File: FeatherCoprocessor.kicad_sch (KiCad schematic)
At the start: 2 parts

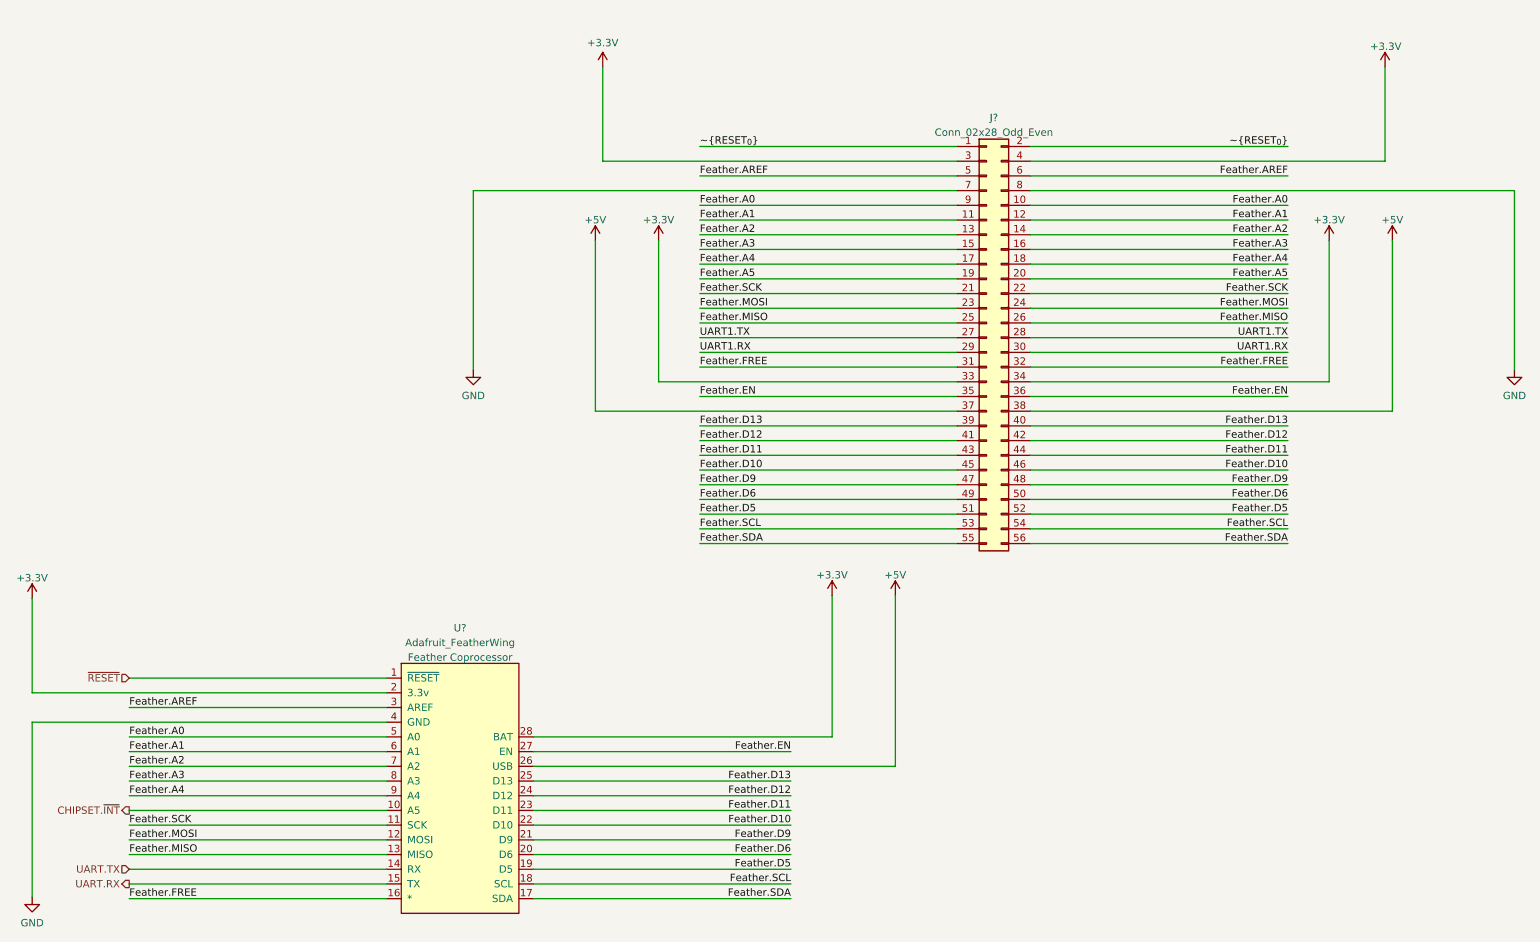
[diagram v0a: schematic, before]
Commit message: Even more simplification and be able to reset feathers separately from the chipset
Makes it possible to also reset them if needed as well
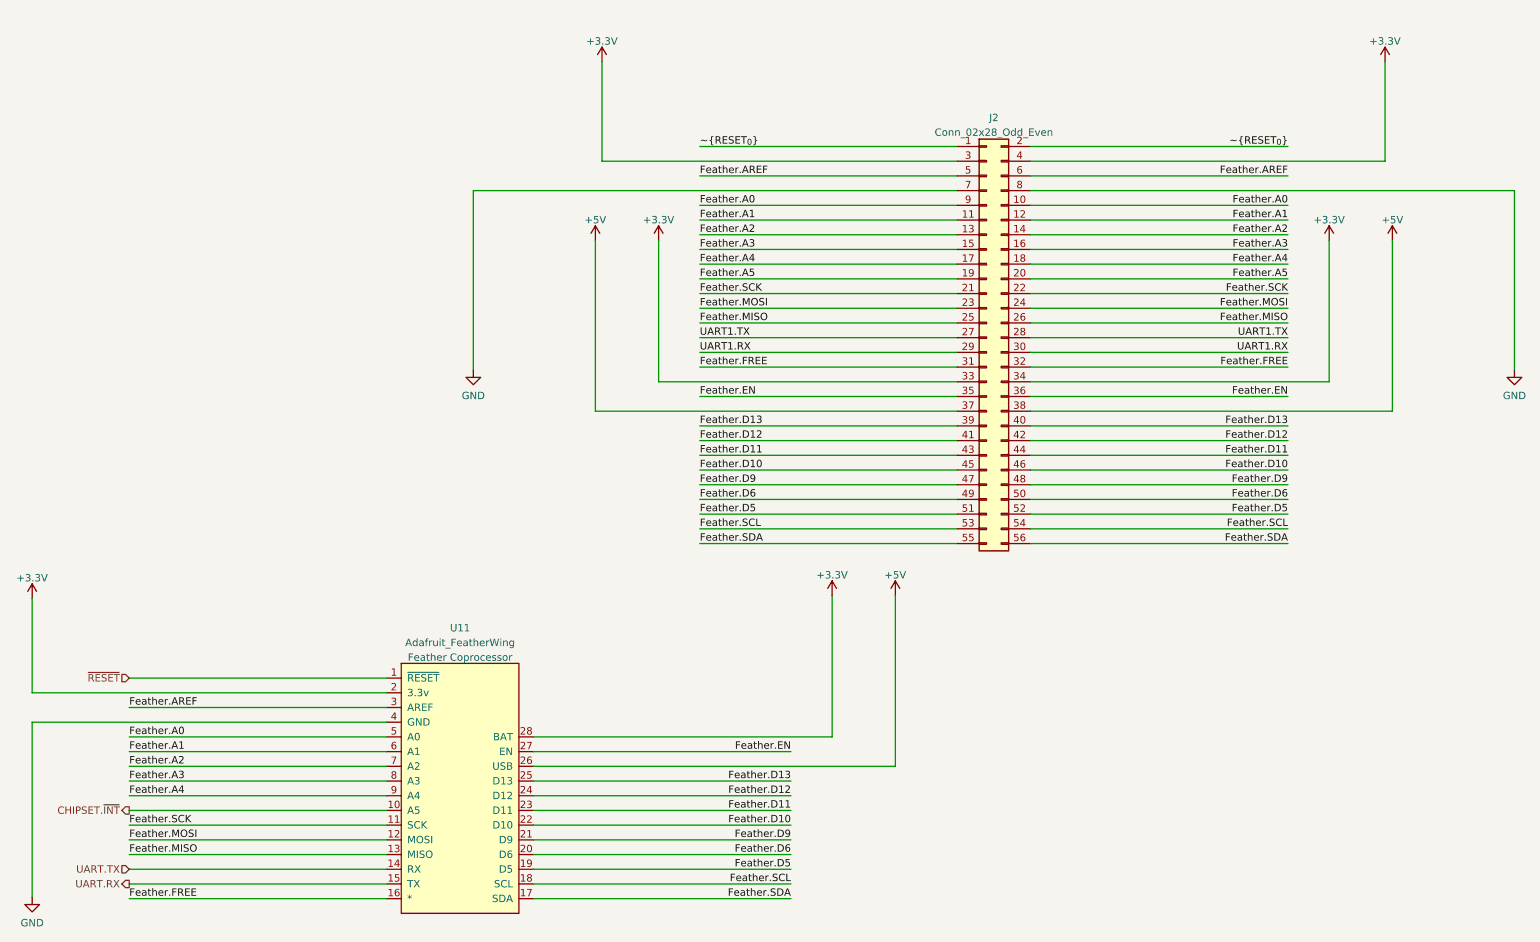
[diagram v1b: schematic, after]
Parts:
- gave numbers to parts that had none: 2
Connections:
- net +3V3 renamed +3.3V

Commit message: Only have one feather
Also came up with a good layout in the form of a "card" style that can
easily be moved around for the i960
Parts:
- removed J2: Conn_02x28_Odd_Even, Connector_PinHeader_2.54mm:PinHeader_2x28_P2.54mm_Vertical, symbol Connector_Generic:Conn_02x28_Odd_Even
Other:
- moved on the sheet: U11

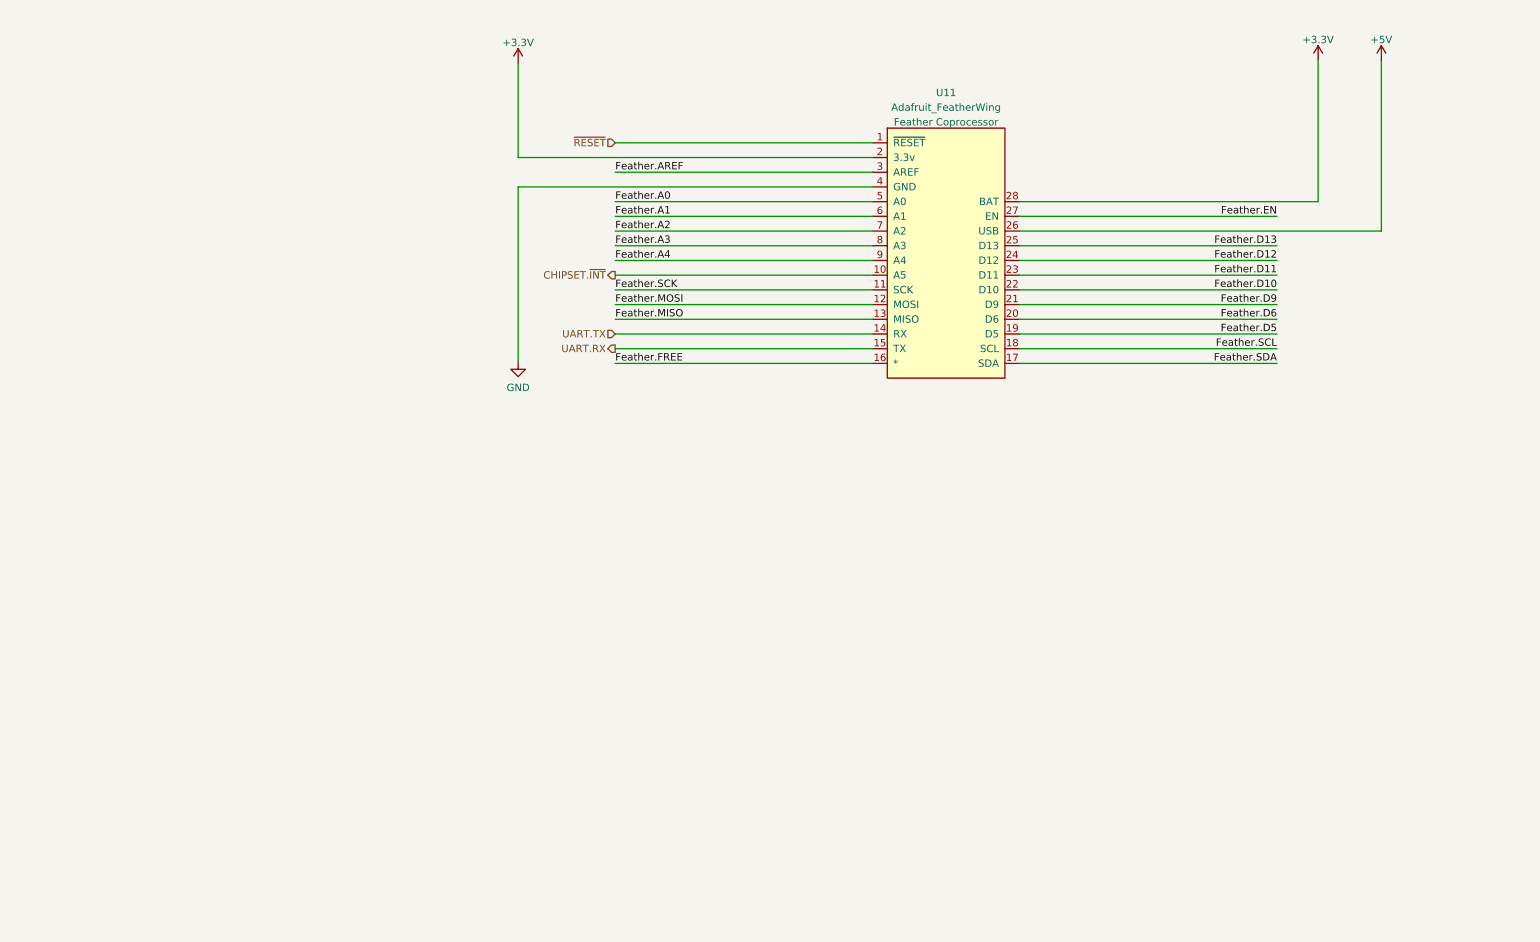
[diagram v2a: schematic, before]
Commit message: Added feather wing sockets next to each plug
F1 has its battery connector blocked by the dazzler shield.

This is not that big of a deal to be honest.
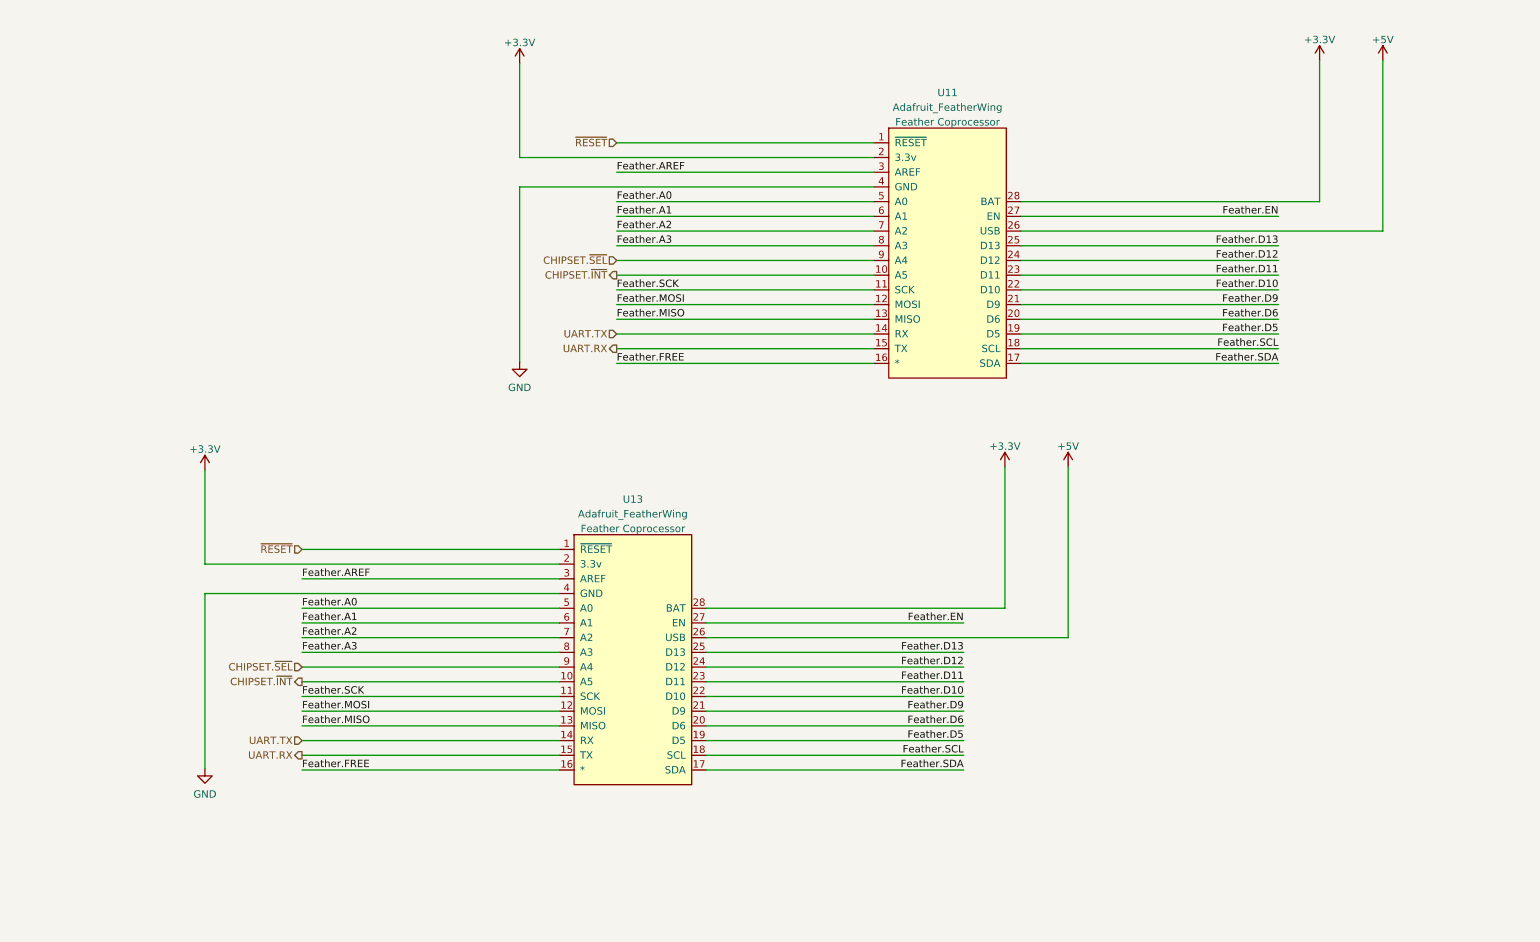
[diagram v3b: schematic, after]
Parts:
- added U13: Adafruit_FeatherWing, Module:Adafruit_Feather, symbol NewICs:Adafruit_FeatherWing
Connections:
- net +3.3V: now also U13.2 (3.3v), U13.28 (BAT)
- net +5V: now also U13.26 (USB)
- net CHIPSET.~{INT}: now also U13.10 (A5)
- net Feather.A0: now also U13.5 (A0)
- net Feather.A1: now also U13.6 (A1)
- net Feather.A2: now also U13.7 (A2)
- net Feather.A3: now also U13.8 (A3)
- net Feather.AREF: now also U13.3 (AREF)
- net Feather.D10: now also U13.22 (D10)
- net Feather.D11: now also U13.23 (D11)
- net Feather.D12: now also U13.24 (D12)
- net Feather.D13: now also U13.25 (D13)
- net Feather.D5: now also U13.19 (D5)
- net Feather.D6: now also U13.20 (D6)
- net Feather.D9: now also U13.21 (D9)
- net Feather.EN: now also U13.27 (EN)
- net Feather.FREE: now also U13.16 (*)
- net Feather.MISO: now also U13.13 (MISO)
- net Feather.MOSI: now also U13.12 (MOSI)
- net Feather.SCK: now also U13.11 (SCK)
- net Feather.SCL: now also U13.18 (SCL)
- net Feather.SDA: now also U13.17 (SDA)
- net GND: now also U13.4 (GND)
- net UART.RX: now also U13.15 (TX)
- net UART.TX: now also U13.14 (RX)
- net ~{RESET}: now also U13.1 (~{RESET})
- net Feather.A4 renamed CHIPSET.~{SEL}
- net CHIPSET.~{SEL}: now also U13.9 (A4)

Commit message: Fix up an issue with 3.3v vs 3v3 power planes
Also, link up more power pads to corresponding power plane
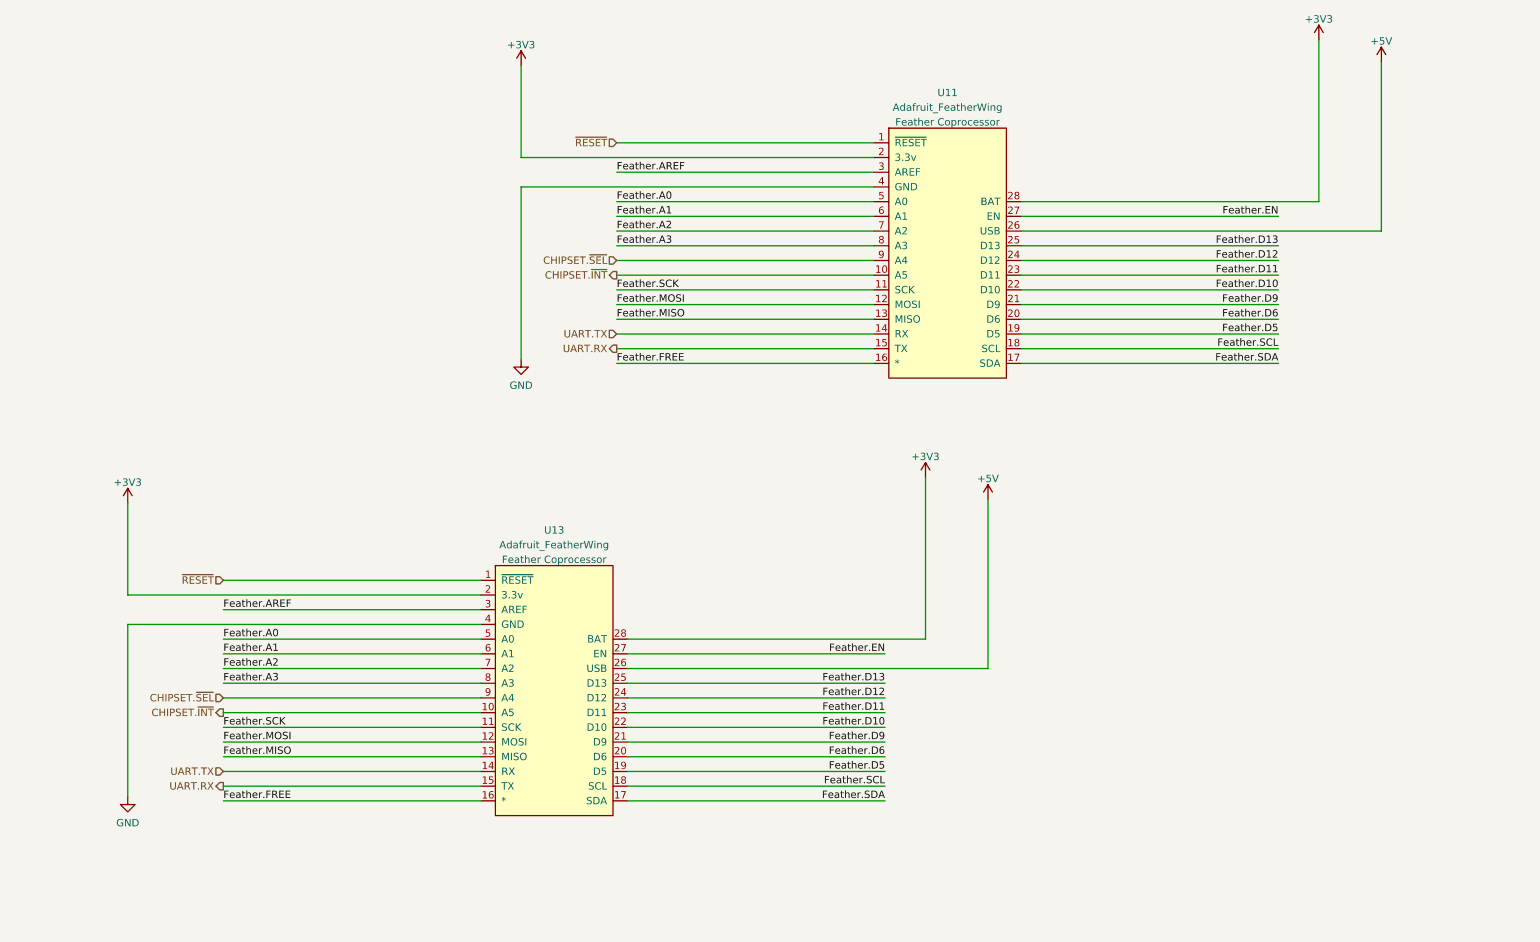
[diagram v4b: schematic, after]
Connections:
- net +3.3V renamed +3V3

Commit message: Added a breakout of the management engine pins
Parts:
- renumbered U13 to U19
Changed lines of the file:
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@@
   (symbol (lib_id "NewICs:Adafruit_FeatherWing") (at 111.76 166.37 0) (unit 1)
     (in_bom yes) (on_board yes) (fields_autoplaced)
-    (property "Reference" "U13" (id 0) (at 111.76 115.8104 0))
+    (property "Reference" "U19" (id 0) (at 111.76 115.8104 0))
     (property "Value" "Adafruit_FeatherWing" (id 1) (at 111.76 118.3473 0))
     (property "Footprint" "Module:Adafruit_Feather" (id 2) (at 111.76 166.37 0)
@@
   (symbol (lib_id "power:GND") (at 38.1 161.925 0) (unit 1)
     (in_bom yes) (on_board yes) (fields_autoplaced)
-    (property "Reference" "#PWR07" (id 0) (at 38.1 168.275 0)
+    (property "Reference" "#PWR015" (id 0) (at 38.1 168.275 0)
       (effects (font (size 1.27 1.27)) hide)
     )
@@
   (symbol (lib_id "power:+5V") (at 186.69 110.49 0) (unit 1)
     (in_bom yes) (on_board yes) (fields_autoplaced)
-    (property "Reference" "#PWR011" (id 0) (at 186.69 114.3 0)
+    (property "Reference" "#PWR018" (id 0) (at 186.69 114.3 0)
       (effects (font (size 1.27 1.27)) hide)
     )
